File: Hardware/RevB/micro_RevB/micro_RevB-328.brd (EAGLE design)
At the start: 50 x 50 mm, 39 parts, among them Q101 CSTCR6M00G53Z, U101 ATMEGA328P, U102 TLC59711, U103 LP2985AIM5-3.3

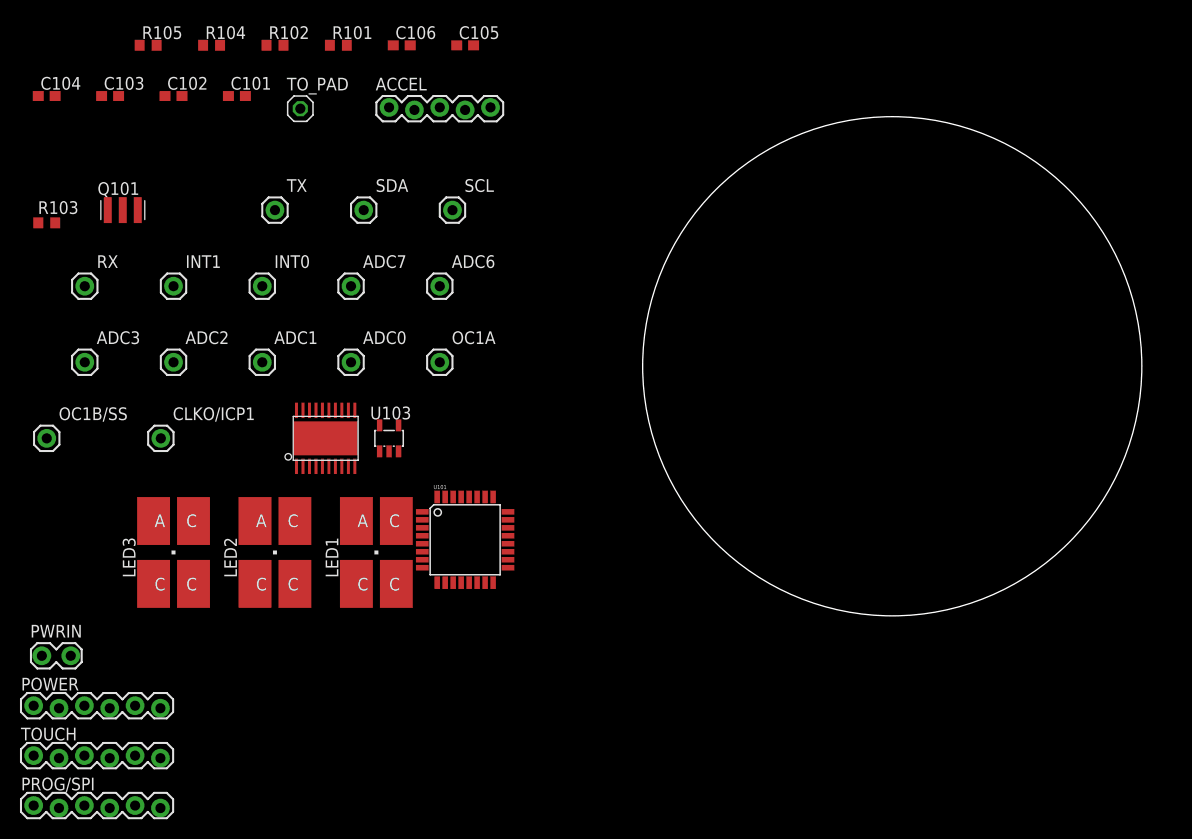
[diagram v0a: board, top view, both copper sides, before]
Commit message: Routing micro RevB
micro RevB is about half routed; schematic had a few errors corrected;
added a notes file to keep track of the things to be kept standard.
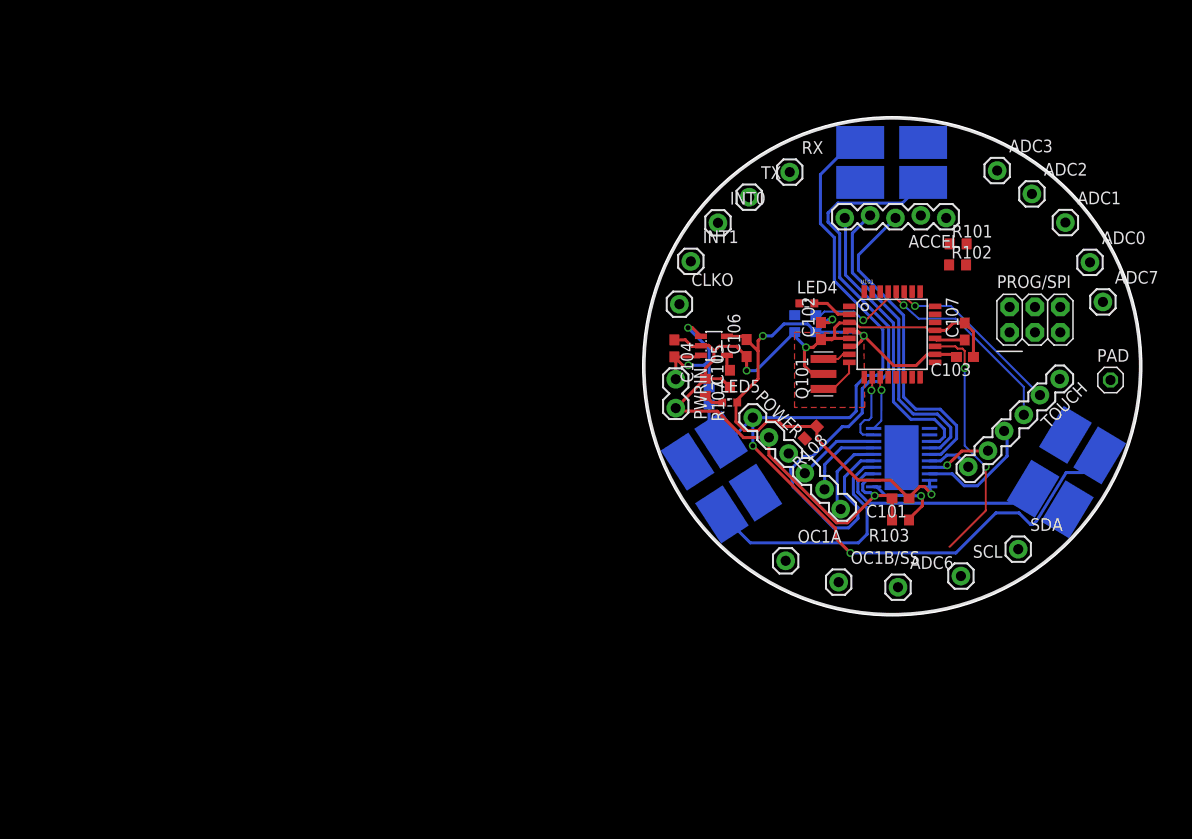
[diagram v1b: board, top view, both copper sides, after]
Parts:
- removed CLKO/ICP1: (no value), SparkFun-Connectors:1X01
- removed TO_PAD: (no value), pinhead:1X01
- added C107: 0.1u, eagle-ltspice:C0603
- added CLKO: (no value), SparkFun-Connectors:1X01
- added LED4, LED5: (no value), led:SML0603
- added PAD: (no value), pinhead:1X01
- added R106, R107: 180, rcl:R0603
- added R108: 0, rcl:R0603
- PROG/SPI: device SparkFun-Connectors:1X06-SIP_LOCK -> SparkFun-Connectors:2X03
- moved PROG/SPI 111.5 mm to (39.3, 29.7)
- moved TOUCH 109.5 mm to (41.8, 23.7), turned to 225 degrees
- moved ADC3 93.4 mm to (35.5, 44.6)
- moved R103 90.6 mm to (25.8, 9.60), turned to 180 degrees
- moved LED3 89.8 mm to (42.4, 14.4), flipped to the bottom, turned to 31 degrees
- moved C103 89.5 mm to (32.3, 25.9), turned to 180 degrees
- moved ADC2 87.6 mm to (39.0, 42.3)
- moved ADC1 81.7 mm to (42.3, 39.4)
- moved OC1B/SS 80.6 mm to (19.6, 3.38)
- moved C101 77.7 mm to (25.8, 11.8), turned to 180 degrees
- moved POWER 77.6 mm to (11.0, 19.9), turned to 315 degrees
- moved ADC7 75.3 mm to (46.1, 31.4)
- moved ADC0 74.7 mm to (44.8, 35.4)
- moved SDA 73.8 mm to (37.6, 6.68)
- moved Q101 72.1 mm to (18.1, 24.2), turned to 90 degrees
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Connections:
- removed net CLKO/ICP1: U101.12
- removed net N$6: LED2.C@4, U102.7
- removed net N$7: LED1.C@4, U102.8
- new net CLKO: CLKO.1, U101.12
- new net M_1: LED1.C@4, U102.5
- new net M_2: LED2.C@4, U102.4
- new net M_3: LED3.C@4, U102.3
- new net N$10: C107.1, U101.20
- new net N$12: LED5.C, R107.2
- new net N$3: LED4.A, U101.2
- new net N$8: LED4.C, R106.2
- net GND: now also C107.2, R106.1, R107.1; no longer U101.20
- net MISO: now also PROG/SPI.1; no longer PROG/SPI.3
- net N$5: now also POWER.3, R108.2; no longer LED3.C@4, U102.6
- net P_1: now also U102.8; no longer U102.5
- net P_2: now also U102.7; no longer U102.4
- net P_3: now also U102.6; no longer U102.3
- net SCK: now also PROG/SPI.3; no longer PROG/SPI.2
- net SDA: now also SDA.1
- net TOUCH: now also PAD.1; no longer TO_PAD.1
- net VCC: now also LED5.A, PROG/SPI.2, R108.1; no longer POWER.3, PROG/SPI.1
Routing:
- net VDD: track 0.00 -> 100.4 mm, vias 0 -> 2
- net GND: track 0.00 -> 91.1 mm, vias 0 -> 3
- net VCC: track 0.00 -> 69.3 mm, vias 0 -> 4
- net M_1: track 0.00 -> 63.2 mm
- net A_1: track 0.00 -> 32.5 mm
- net A_2: track 0.00 -> 31.0 mm
- net A_3: track 0.00 -> 29.1 mm
- net ADC6: track 0.00 -> 25.2 mm, vias 0 -> 2
- net M_2: track 0.00 -> 24.7 mm
- net M_3: track 0.00 -> 21.6 mm
- net SCL: track 0.00 -> 19.9 mm, vias 0 -> 1
- net SDA: track 0.00 -> 18.2 mm, vias 0 -> 1
- net VEE: track 0.00 -> 17.6 mm, vias 0 -> 2
- net T_1: track 0.00 -> 12.1 mm
- net RST: track 0.00 -> 9.31 mm, vias 0 -> 1
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- added copper zone on layer 1, net GND

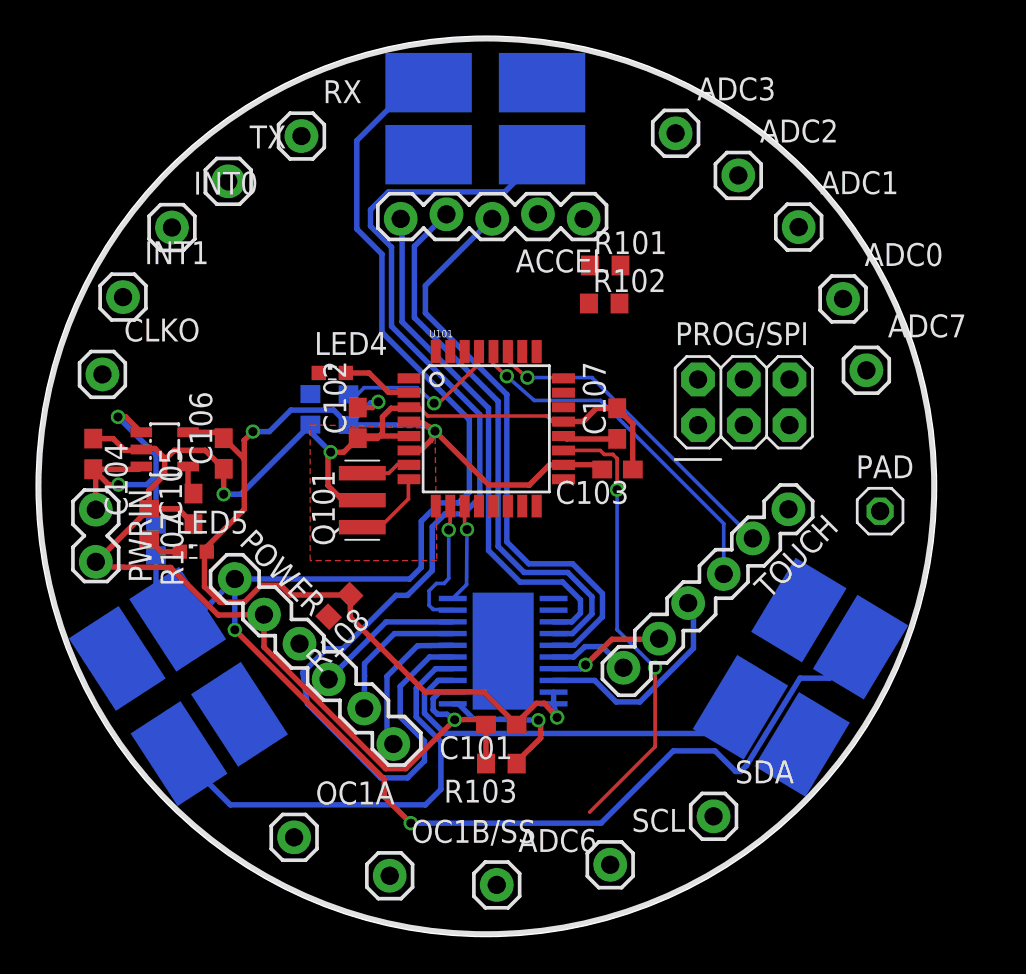
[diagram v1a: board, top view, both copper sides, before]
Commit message: Progress on routing micron RevB
Done routing; working on the silkcreening; probably changing the ADC
individual pins to a 5 pin header.
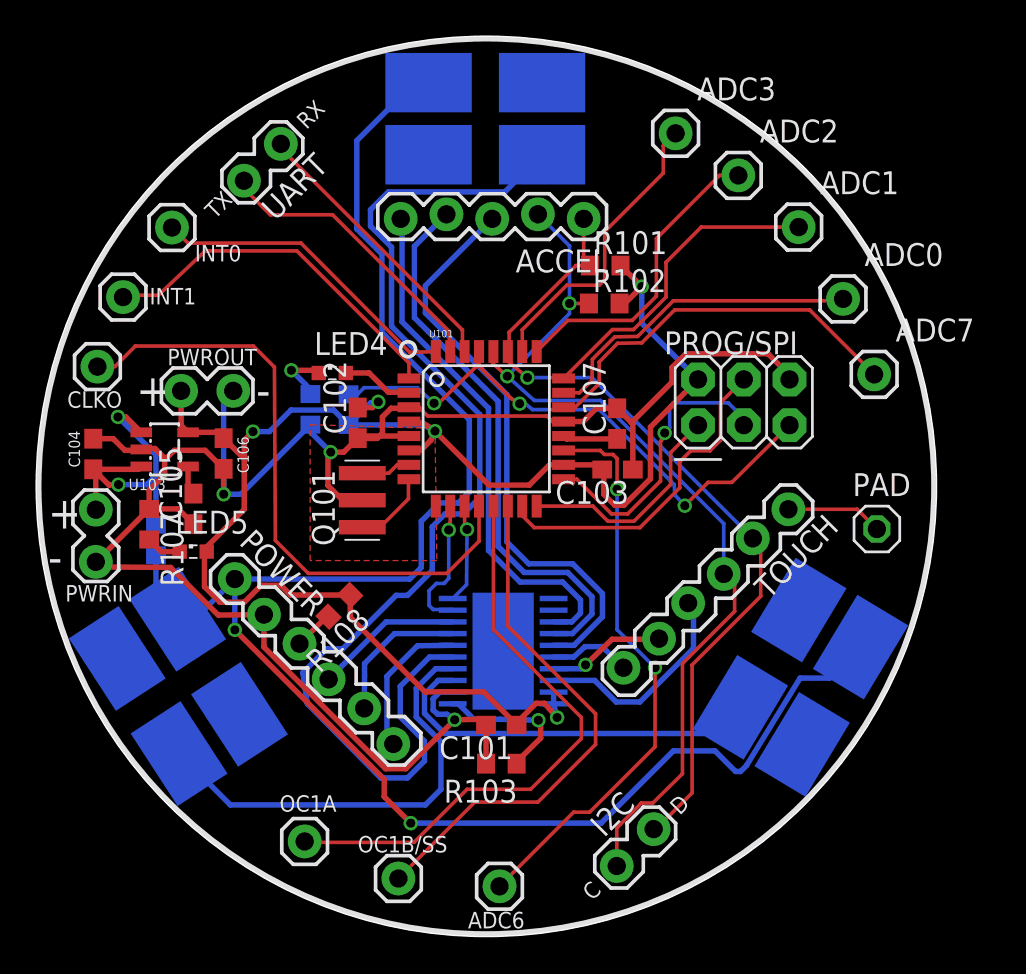
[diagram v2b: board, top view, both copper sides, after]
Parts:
- removed RX, SCL, SDA, TX: (no value), SparkFun-Connectors:1X01
- added I2C, PWROUT, UART: (no value), SparkFun-Connectors:1X02_LOCK
- moved PAD 1.01 mm to (46.7, 22.6)
- moved OC1A 0.63 mm to (14.9, 5.28)
- moved CLKO 0.51 mm to (3.40, 31.6)
- moved OC1B/SS 0.51 mm to (20.1, 3.23)
- moved ADC7 0.49 mm to (46.5, 31.2)
- moved ADC6 0.17 mm to (25.7, 2.79)
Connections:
- removed net GND: C101.2, C102.1, C103.1, C104.1, C105.1, C106.1, C107.2, POWER.2, PROG/SPI.6, PWRIN.2, Q101.2, R103.2, R106.1, R107.1, U101.21, U101.3, U101.5, U102.2, U103.2
- new net N7: C101.2, C102.1, C103.1, C104.1, C105.1, C106.1, C107.2, POWER.2, PROG/SPI.6, PWRIN.2, PWROUT.2, Q101.2, R103.2, R106.1, R107.1, U101.21, U101.3, U101.5, U102.2, U103.2
- net RX: now also UART.1; no longer RX.1
- net SCL: now also I2C.2; no longer SCL.1
- net SDA: now also I2C.1; no longer SDA.1
- net TX: now also UART.2; no longer TX.1
- net VCC: now also PWROUT.1
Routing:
- net N7: track 0.00 -> 108.7 mm, vias 0 -> 3
- net GND: track 91.1 -> 0.00 mm, vias 3 -> 0
- net CLKO: track 0.00 -> 35.2 mm
- net OC1A: track 0.00 -> 32.7 mm
- net SCL: track 19.9 -> 51.7 mm, vias 1 -> 2
- net OC1B/SS: track 0.00 -> 29.3 mm
- net SDA: track 18.2 -> 46.9 mm
- net VCC: track 69.3 -> 93.0 mm, vias 4 -> 5
- net RST: track 9.31 -> 32.7 mm, vias 1 -> 3
- net ADC7: track 0.00 -> 21.7 mm
- net INT1: track 0.00 -> 20.3 mm
- net MOSI: track 0.00 -> 18.6 mm
- net ADC0: track 0.00 -> 18.3 mm
- net ADC1: track 0.00 -> 17.7 mm
- net INT0: track 0.00 -> 17.5 mm
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- added copper zone on layer 1, net N7
- removed copper zone on layer 1, net GND
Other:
- board text added: "+"
- board text added: "-"
- board text added: "C"
- board text added: "D"
- board text added: "RX"
- board text added: "TX"
- board text added: "U103"
